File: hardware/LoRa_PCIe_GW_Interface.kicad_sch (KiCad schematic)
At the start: 45 parts, among them U300 RP2040, U301 GD25Q16EEIGR, Y300 12 MHz

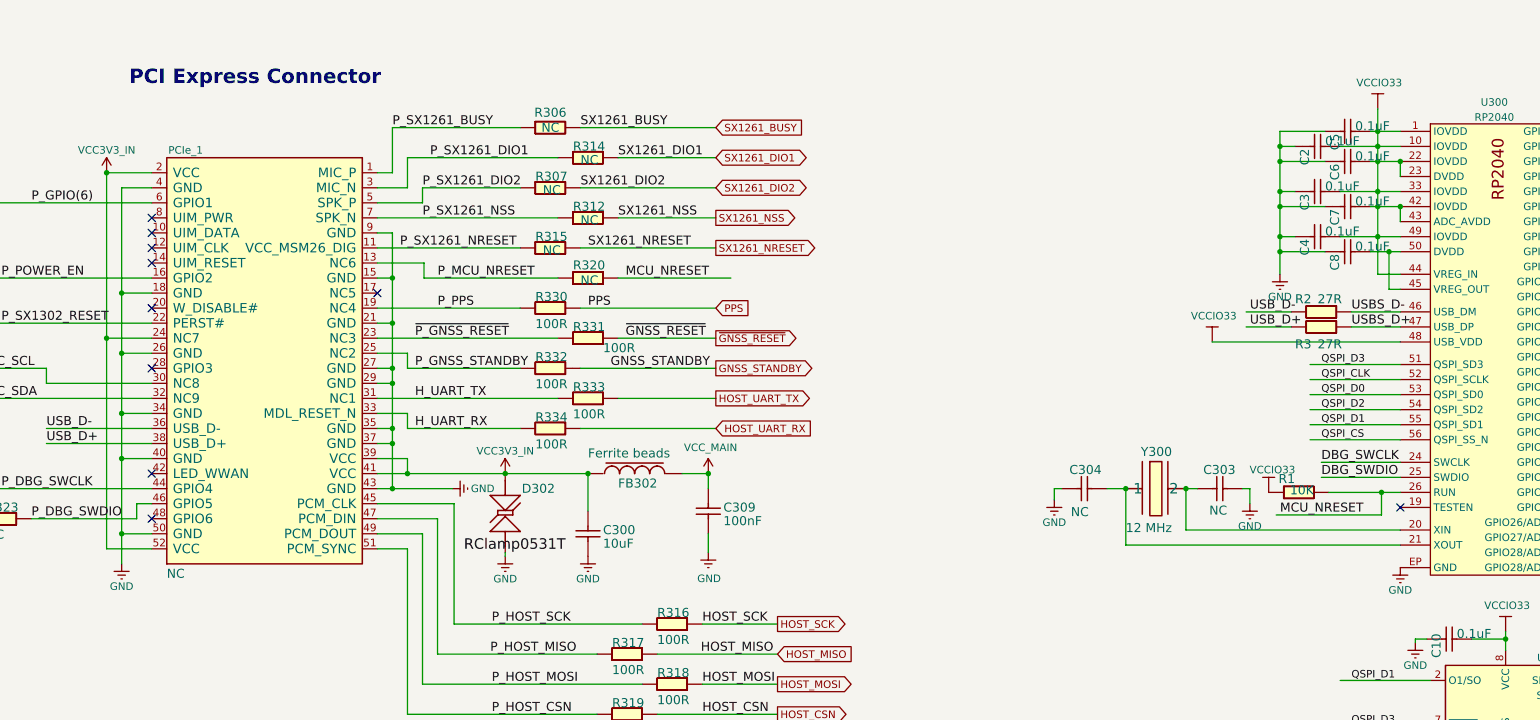
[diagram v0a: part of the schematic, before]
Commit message: Fixed DRC errors and warnings. Improved manufacturing quality.
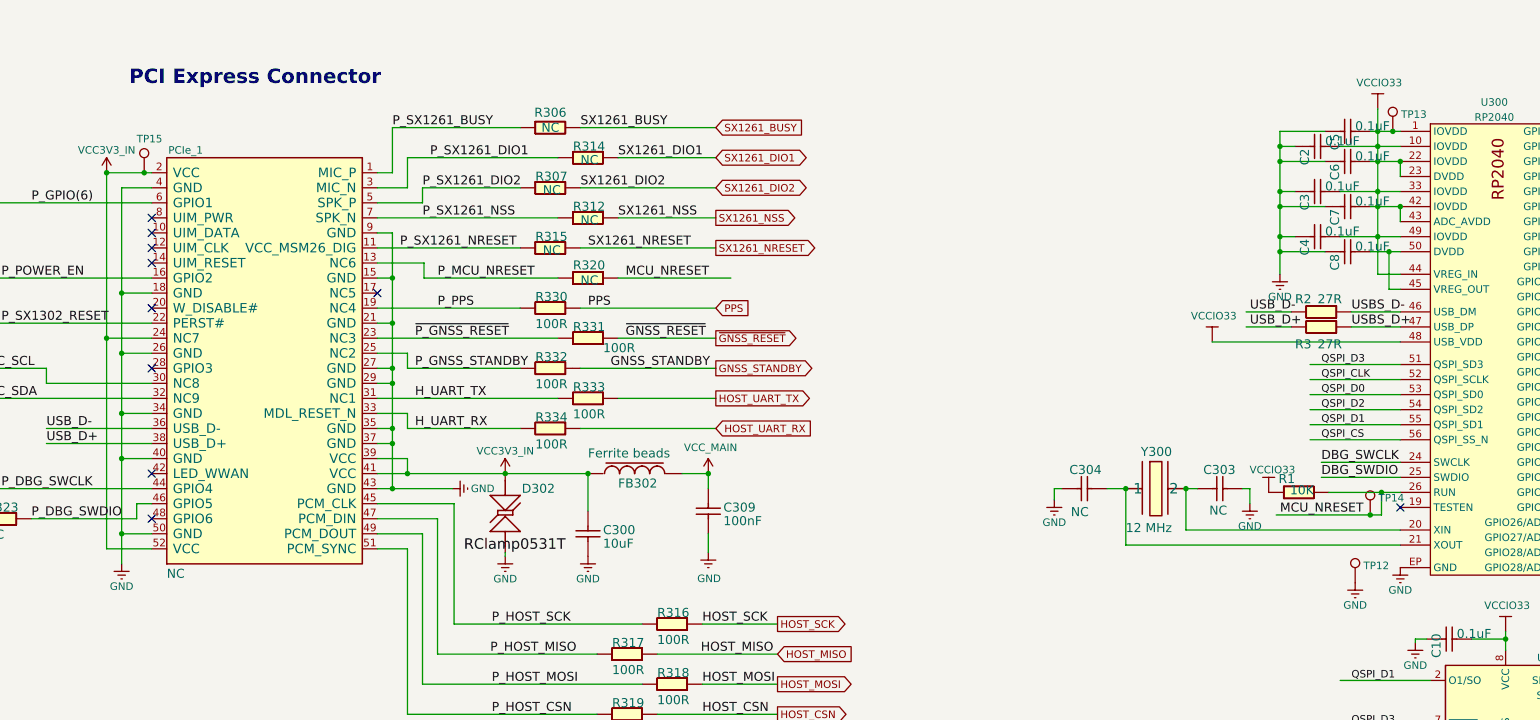
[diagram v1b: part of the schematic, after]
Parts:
- added TP12, TP13, TP14, TP15: TestPoint, nebra:TestPoint_SMD_1.6mm, symbol Connector:TestPoint
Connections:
- net GND: now also TP12.1
- net MCU_NRESET: now also TP14.1
- net VCC3V3_IN: now also TP15.1
- net VCCIO33: now also TP13.1
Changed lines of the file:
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@@
   (junction (at 85.09 90.805) (diameter 0) (color 0 0 0 0)
   )
+  (junction (at 302.26 83.82) (diameter 0) (color 0 0 0 0)
+  )
   (junction (at 299.72 96.52) (diameter 0) (color 0 0 0 0)
   )
@@
   (junction (at 299.72 86.36) (diameter 0) (color 0 0 0 0)
   )
+  (junction (at 298.45 148.59) (diameter 0) (color 0 0 0 0)
+  )
   (junction (at 299.72 101.6) (diameter 0) (color 0 0 0 0)
   )
   (junction (at 35.56 149.225) (diameter 0) (color 0 0 0 0)
+  )
+  (junction (at 91.44 90.805) (diameter 0) (color 0 0 0 0)
   )
   (junction (at 87.63 139.065) (diameter 0) (color 0 0 0 0)
@@
     (stroke (width 0) (type default) (color 0 0 0 0))
   )
-  (wire (pts (xy 282.575 148.59) (xy 300.355 148.59))
+  (wire (pts (xy 282.575 148.59) (xy 298.45 148.59))
     (stroke (width 0) (type default) (color 0 0 0 0))
   )
@@
     (stroke (width 0) (type default) (color 0 0 0 0))
   )
-  (wire (pts (xy 299.72 83.82) (xy 303.53 83.82))
+  (wire (pts (xy 299.72 83.82) (xy 302.26 83.82))
     (stroke (width 0) (type default) (color 0 0 0 0))
   )
@@
     (stroke (width 0) (type default) (color 0 0 0 0))
   )
+  (wire (pts (xy 85.09 90.805) (xy 91.44 90.805))
+    (stroke (width 0) (type default) (color 0 0 0 0))
+  )
   (wire (pts (xy 299.72 86.36) (xy 299.72 88.9))
     (stroke (width 0) (type default) (color 0 0 0 0))
@@
     (stroke (width 0) (type default) (color 0 0 0 0))
   )
+  (wire (pts (xy 138.684 108.585) (xy 161.29 108.585))
+    (stroke (width 0) (type default) (color 0 0 0 0))
+  )
   (wire (pts (xy 133.35 100.965) (xy 130.81 100.965))
     (stroke (width 0) (type default) (color 0 0 0 0))
@@
     (stroke (width 0) (type default) (color 0 0 0 0))
   )
+  (wire (pts (xy 91.44 90.805) (xy 92.71 90.805))
+    (stroke (width 0) (type default) (color 0 0 0 0))
+  )
   (wire (pts (xy 353.06 86.36) (xy 335.28 86.36))
     (stroke (width 0) (type default) (color 0 0 0 0))
@@
     (stroke (width 0) (type default) (color 0 0 0 0))
   )
-  (wire (pts (xy 138.684 108.585) (xy 161.29 108.585))
-    (stroke (width 0) (type default) (color 0 0 0 0))
-  )
   (wire (pts (xy 45.72 123.825) (xy 36.83 123.825))
     (stroke (width 0) (type default) (color 0 0 0 0))
@@
     (stroke (width 0) (type default) (color 0 0 0 0))
   )
+  (wire (pts (xy 302.26 83.82) (xy 303.53 83.82))
+    (stroke (width 0) (type default) (color 0 0 0 0))
+  )
   (wire (pts (xy 290.195 139.7) (xy 303.53 139.7))
     (stroke (width 0) (type default) (color 0 0 0 0))
@@
     (stroke (width 0) (type default) (color 0 0 0 0))
   )
+  (wire (pts (xy 298.45 148.59) (xy 300.355 148.59))
+    (stroke (width 0) (type default) (color 0 0 0 0))
+  )
   (wire (pts (xy 31.75 149.225) (xy 35.56 149.225))
     (stroke (width 0) (type default) (color 0 0 0 0))
@@
   )
   (wire (pts (xy 307.975 169.545) (xy 306.07 169.545))
-    (stroke (width 0) (type default) (color 0 0 0 0))
-  )
-  (wire (pts (xy 85.09 90.805) (xy 92.71 90.805))
     (stroke (width 0) (type default) (color 0 0 0 0))
   )
@@
     (pin "1")
   )
+  (symbol (lib_id "Connector:TestPoint") (at 302.26 83.82 0) (unit 1)
+    (in_bom yes) (on_board yes) (fields_autoplaced)
+    (property "Reference" "TP13" (id 0) (at 303.657 80.9518 0)
+      (effects (font (size 1.27 1.27)) (justify left))
+    )
+    (property "Value" "TestPoint" (id 1) (at 303.657 82.2202 0)
+      (effects (font (size 1.27 1.27)) (justify left) hide)
+    )
+    (property "Footprint" "nebra:TestPoint_SMD_1.6mm" (id 2) (at 307.34 83.82 0)
+      (effects (font (size 1.27 1.27)) hide)
+    )
+    (property "Datasheet" "~" (id 3) (at 307.34 83.82 0)
+      (effects (font (size 1.27 1.27)) hide)
+    )
+    (pin "1")
+  )
   (symbol (lib_id "LoRa_PCIe_GW-rescue:GND") (at 283.21 107.95 0) (unit 1)
     (in_bom yes) (on_board yes)
@@
     )
     (property "Datasheet" "" (id 3) (at 278.765 142.24 0)
+      (effects (font (size 1.27 1.27)) hide)
+    )
+    (pin "1")
+  )
+  (symbol (lib_id "Connector:TestPoint") (at 91.44 90.805 0) (unit 1)
+    (in_bom yes) (on_board yes)
+    (property "Reference" "TP15" (id 0) (at 90.17 85.09 0)
+      (effects (font (size 1.27 1.27)) (justify left))
+    )
+    (property "Value" "TestPoint" (id 1) (at 92.837 89.2052 0)
+      (effects (font (size 1.27 1.27)) (justify left) hide)
+    )
+    (property "Footprint" "nebra:TestPoint_SMD_1.6mm" (id 2) (at 96.52 90.805 0)
+      (effects (font (size 1.27 1.27)) hide)
+    )
+    (property "Datasheet" "~" (id 3) (at 96.52 90.805 0)
       (effects (font (size 1.27 1.27)) hide)
     )
@@
     )
     (property "Datasheet" "" (id 3) (at 297.18 77.47 0)
+      (effects (font (size 1.27 1.27)) hide)
+    )
+    (pin "1")
+  )
+  (symbol (lib_id "LoRa_PCIe_GW-rescue:GND") (at 295.91 160.02 0) (unit 1)
+    (in_bom yes) (on_board yes)
+    (property "Reference" "#PWR03" (id 0) (at 295.91 156.845 0)
+      (effects (font (size 1.27 1.27)) hide)
+    )
+    (property "Value" "GND" (id 1) (at 295.91 163.83 0))
+    (property "Footprint" "" (id 2) (at 290.83 160.02 0)
+      (effects (font (size 1.27 1.27)) hide)
+    )
+    (property "Datasheet" "" (id 3) (at 290.83 160.02 0)
       (effects (font (size 1.27 1.27)) hide)
     )
@@
     (pin "2")
   )
+  (symbol (lib_id "Connector:TestPoint") (at 298.45 148.59 0) (unit 1)
+    (in_bom yes) (on_board yes) (fields_autoplaced)
+    (property "Reference" "TP14" (id 0) (at 299.847 145.7218 0)
+      (effects (font (size 1.27 1.27)) (justify left))
+    )
+    (property "Value" "TestPoint" (id 1) (at 299.847 146.9902 0)
+      (effects (font (size 1.27 1.27)) (justify left) hide)
+    )
+    (property "Footprint" "nebra:TestPoint_SMD_1.6mm" (id 2) (at 303.53 148.59 0)
+      (effects (font (size 1.27 1.27)) hide)
+    )
+    (property "Datasheet" "~" (id 3) (at 303.53 148.59 0)
+      (effects (font (size 1.27 1.27)) hide)
+    )
+    (pin "1")
+  )
+  (symbol (lib_id "Connector:TestPoint") (at 295.91 160.02 0) (unit 1)
+    (in_bom yes) (on_board yes) (fields_autoplaced)
+    (property "Reference" "TP12" (id 0) (at 297.307 157.1518 0)
+      (effects (font (size 1.27 1.27)) (justify left))
+    )
+    (property "Value" "TestPoint" (id 1) (at 297.307 158.4202 0)
+      (effects (font (size 1.27 1.27)) (justify left) hide)
+    )
+    (property "Footprint" "nebra:TestPoint_SMD_1.6mm" (id 2) (at 300.99 160.02 0)
+      (effects (font (size 1.27 1.27)) hide)
+    )
+    (property "Datasheet" "~" (id 3) (at 300.99 160.02 0)
+      (effects (font (size 1.27 1.27)) hide)
+    )
+    (pin "1")
+  )
 )

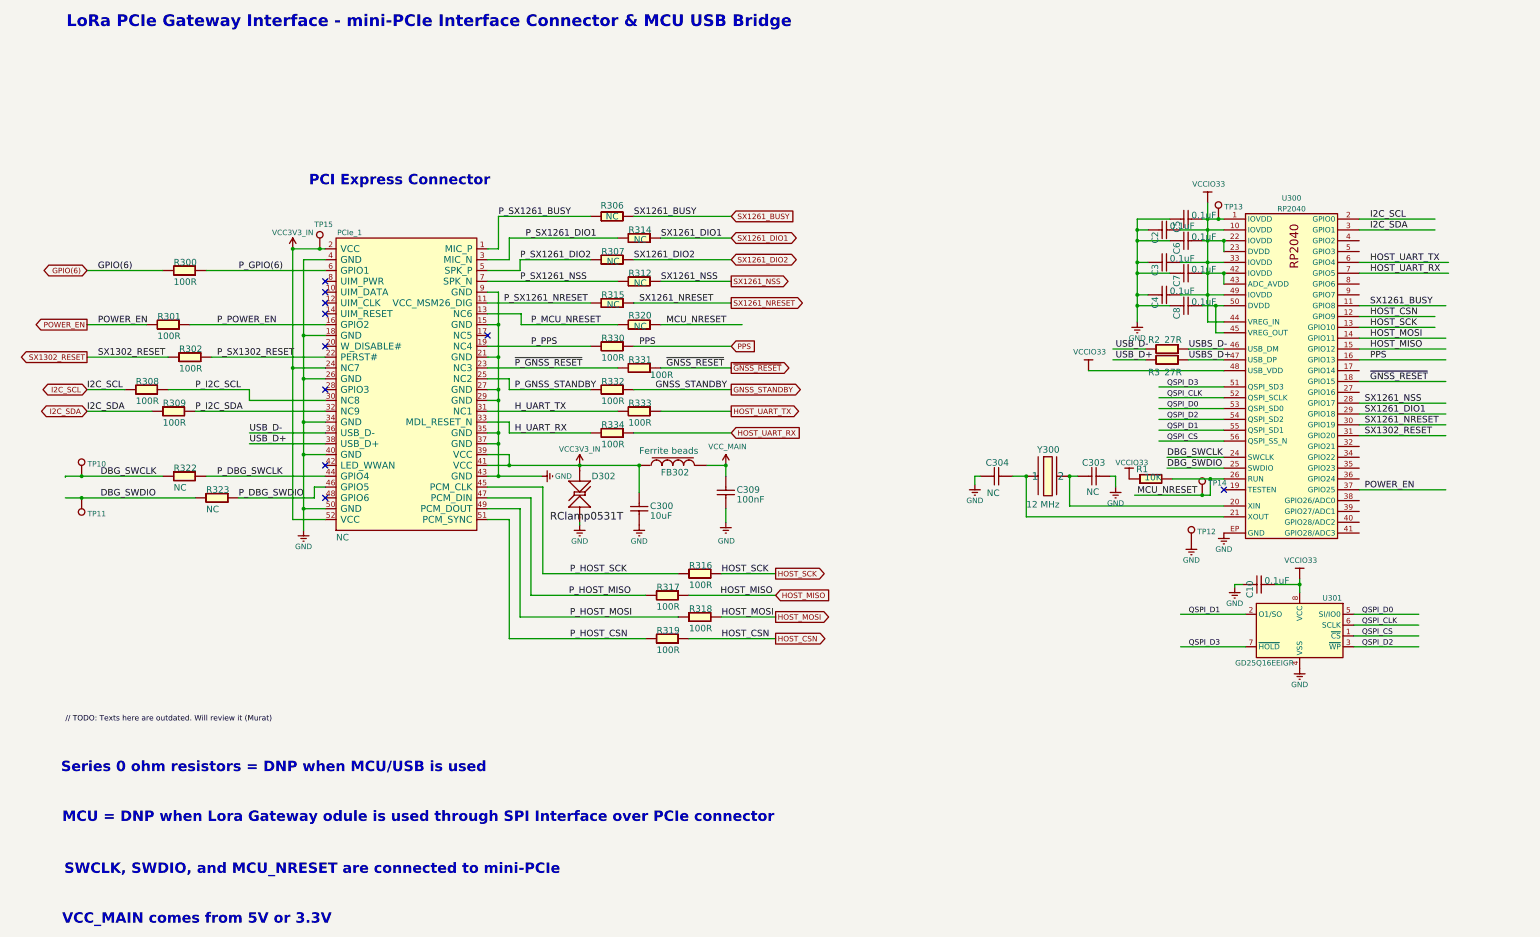
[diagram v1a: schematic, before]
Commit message: Fixed couple of IO position issues. Controlled everything again.
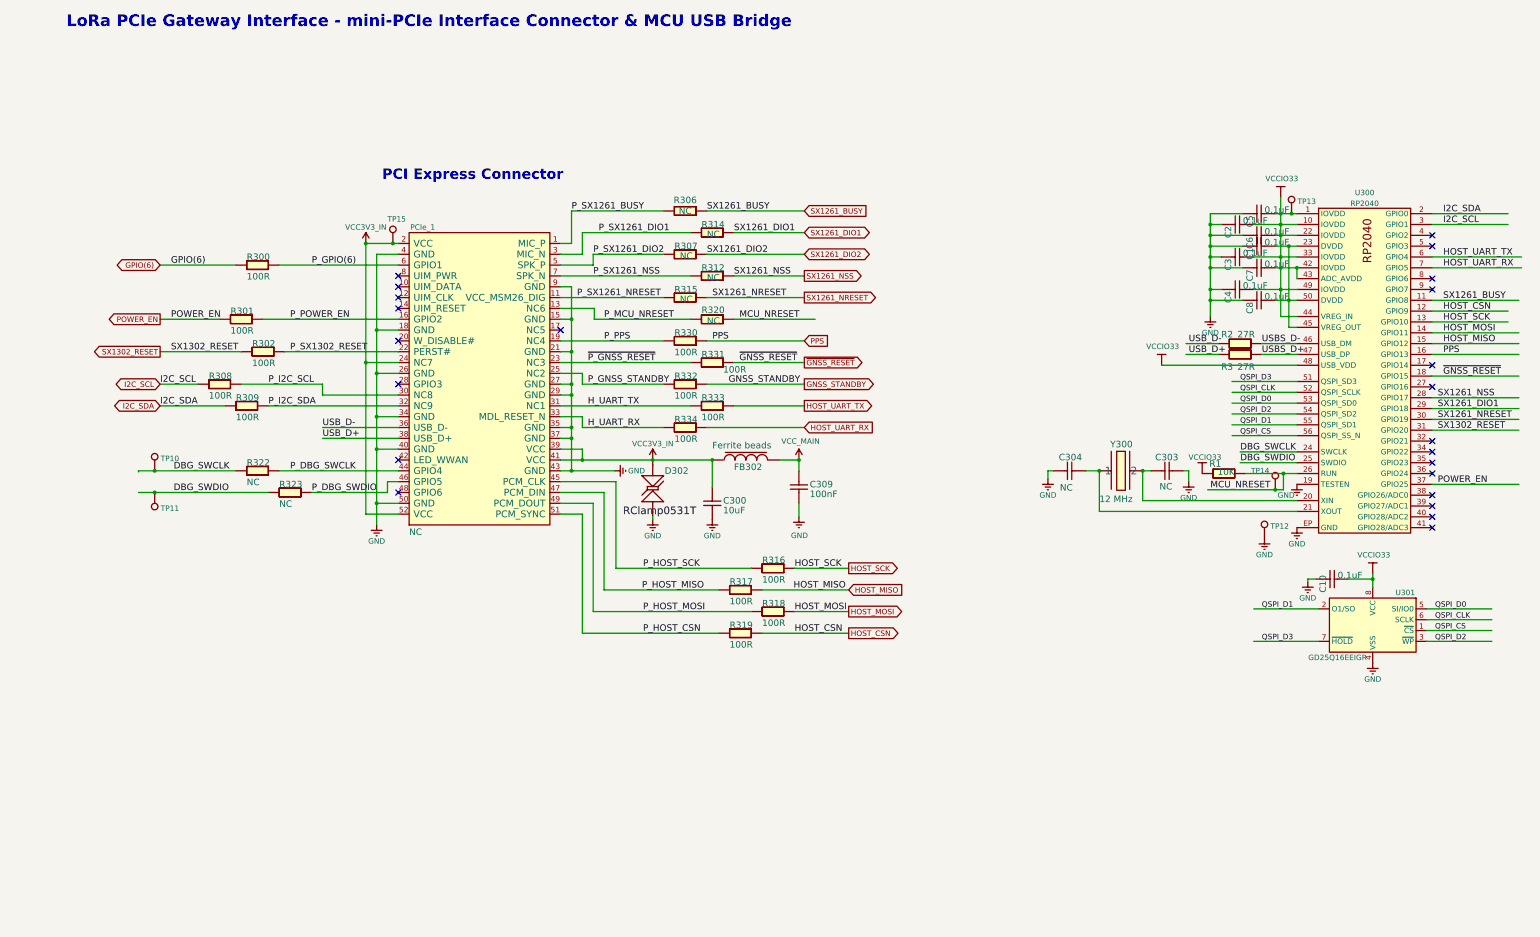
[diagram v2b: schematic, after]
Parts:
- added C1: 0.1uF, LoRa_PCIe_GW:rlc_402_smd_small, symbol LoRa_PCIe_GW-rescue:Cap-
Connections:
- net GND: now also U300.19 (TESTEN), C1.2
- net I2C_SCL: now also U300.3 (GPIO1); no longer U300.2 (GPIO0)
- net I2C_SDA: now also U300.2 (GPIO0); no longer U300.3 (GPIO1)
- net VCCIO33: no longer U300.23 (DVDD)
- net at C8.1, U300.45 (VREG_OUT), U300.50 (DVDD): now also U300.23 (DVDD), C1.1
- no-connect marks 10 -> 23
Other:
- note removed: "MCU = DNP when Lora Gateway odule is used through SPI Interface over PCIe connector"
- note removed: "SWCLK, SWDIO, and MCU_NRESET are connected to mini-PCIe"
- note removed: "Series 0 ohm resistors = DNP when MCU/USB is used"
- note removed: "VCC_MAIN comes from 5V or 3.3V"
- moved on the sheet: C10, C2, C3, C300, C303, C304, C309, C4, C5, C6, C7, C8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

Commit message: Fixed ERC and Schematic to Layout parity errors.
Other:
- note added: "RClamp0531T"
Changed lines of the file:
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@@
   (junction (at 52.705 142.875) (diameter 0) (color 0 0 0 0)
+  )
+  (junction (at 158.115 140.335) (diameter 0) (color 0 0 0 0)
   )
   (junction (at 300.355 90.17) (diameter 0) (color 0 0 0 0)
@@
     (stroke (width 0) (type default) (color 0 0 0 0))
   )
+  (wire (pts (xy 158.115 140.335) (xy 169.545 140.335))
+    (stroke (width 0) (type default) (color 0 0 0 0))
+  )
   (wire (pts (xy 192.659 175.895) (xy 155.575 175.895))
     (stroke (width 0) (type default) (color 0 0 0 0))
@@
     (stroke (width 0) (type default) (color 0 0 0 0))
   )
-  (wire (pts (xy 153.035 140.335) (xy 169.545 140.335))
+  (wire (pts (xy 153.035 140.335) (xy 158.115 140.335))
     (stroke (width 0) (type default) (color 0 0 0 0))
   )
@@
   (wire (pts (xy 332.74 168.275) (xy 338.455 168.275))
     (stroke (width 0) (type default) (color 0 0 0 0))
+  )
+  (text "RClamp0531T" (at 166.37 157.48 90)
+    (effects (font (size 1.27 1.27)) (justify left bottom))
   )
   (text "LoRa PCIe Gateway Interface - mini-PCIe Interface Connector & MCU USB Bridge"
@@
   (label "HOST_MISO" (at 354.965 113.03 0)
     (effects (font (size 1.524 1.524)) (justify left bottom))
-  )
-  (label "RClamp0531T" (at 162.56 153.67 0)
-    (effects (font (size 1.778 1.778)) (justify left bottom))
   )
   (label "P_HOST_SCK" (at 167.259 165.735 0)
@@
     (pin "7")
     (pin "8")
+    (pin "9")
+  )
+  (symbol (lib_id "power:PWR_FLAG") (at 203.835 140.335 270) (unit 1)
+    (in_bom yes) (on_board yes) (fields_autoplaced)
+    (property "Reference" "#FLG0103" (id 0) (at 205.74 140.335 0)
+      (effects (font (size 1.27 1.27)) hide)
+    )
+    (property "Value" "PWR_FLAG" (id 1) (at 207.01 140.7688 90)
+      (effects (font (size 1.27 1.27)) (justify left))
+    )
+    (property "Footprint" "" (id 2) (at 203.835 140.335 0)
+      (effects (font (size 1.27 1.27)) hide)
+    )
+    (property "Datasheet" "~" (id 3) (at 203.835 140.335 0)
+      (effects (font (size 1.27 1.27)) hide)
+    )
+    (pin "1")
   )
   (symbol (lib_id "Connector:TestPoint") (at 52.705 147.955 180) (unit 1)
@@
       (effects (font (size 1.27 1.27)) hide)
     )
+    (pin "1")
+  )
+  (symbol (lib_id "power:PWR_FLAG") (at 158.115 140.335 0) (unit 1)
+    (in_bom yes) (on_board yes) (fields_autoplaced)
+    (property "Reference" "#FLG0102" (id 0) (at 158.115 138.43 0)
+      (effects (font (size 1.27 1.27)) hide)
+    )
+    (property "Value" "PWR_FLAG" (id 1) (at 158.115 136.7592 0))
+    (property "Footprint" "" (id 2) (at 158.115 140.335 0)
+      (effects (font (size 1.27 1.27)) hide)
+    )
+    (property "Datasheet" "~" (id 3) (at 158.115 140.335 0)
+      (effects (font (size 1.27 1.27)) hide)
+    )
